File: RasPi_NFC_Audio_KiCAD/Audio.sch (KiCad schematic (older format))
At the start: 14 parts

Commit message: Schematic update
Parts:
- removed J?: SPKR0, Connector_PinHeader_2.54mm:PinHeader_1x02_P2.54mm_Vertical, symbol Connector_Generic:Conn_01x02
- removed J?: SPKR1, Connector_PinHeader_2.54mm:PinHeader_1x02_P2.54mm_Vertical, symbol Connector_Generic:Conn_01x02
- added J? (x2): Screw_Terminal_01x02, symbol Connector:Screw_Terminal_01x02
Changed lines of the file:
@@
 NoConn ~ 4590 2530
 $Comp
-L power:GND #PWR?
+L power:GND #PWR0134
 U 1 1 5ACDFE68
 P 5490 3280
-F 0 "#PWR?" H 5490 3030 50  0001 C CNN
+F 0 "#PWR0134" H 5490 3030 50  0001 C CNN
 F 1 "GND" H 5490 3130 50  0000 C CNN
 F 2 "" H 5490 3280 50  0001 C CNN
@@
 $EndComp
 $Comp
-L power:+5V #PWR?
+L power:+5V #PWR0135
 U 1 1 5ACDFE6E
 P 5540 1080
-F 0 "#PWR?" H 5540 930 50  0001 C CNN
+F 0 "#PWR0135" H 5540 930 50  0001 C CNN
 F 1 "+5V" H 5540 1220 50  0000 C CNN
 F 2 "" H 5540 1080 50  0001 C CNN
@@
 $EndComp
 $Comp
-L power:GND #PWR?
+L power:GND #PWR0136
 U 1 1 5ACDFE90
 P 3570 2440
-F 0 "#PWR?" H 3570 2190 50  0001 C CNN
+F 0 "#PWR0136" H 3570 2190 50  0001 C CNN
 F 1 "GND" H 3570 2290 50  0000 C CNN
 F 2 "" H 3570 2440 50  0001 C CNN
@@
 $EndComp
 $Comp
-L power:+5V #PWR?
+L power:+5V #PWR0137
 U 1 1 5ACDFE96
 P 3570 1640
-F 0 "#PWR?" H 3570 1490 50  0001 C CNN
+F 0 "#PWR0137" H 3570 1490 50  0001 C CNN
 F 1 "+5V" H 3570 1780 50  0000 C CNN
 F 2 "" H 3570 1640 50  0001 C CNN
@@
 $EndComp
 $Comp
-L power:GND #PWR?
+L power:GND #PWR0138
 U 1 1 5AD12414
 P 5820 1450
-F 0 "#PWR?" H 5820 1200 50  0001 C CNN
+F 0 "#PWR0138" H 5820 1200 50  0001 C CNN
 F 1 "GND" H 5820 1300 50  0000 C CNN
 F 2 "" H 5820 1450 50  0001 C CNN
@@
 $EndComp
 $Comp
-L power:GND #PWR?
+L power:GND #PWR0139
 U 1 1 5AD125D7
 P 6150 1460
-F 0 "#PWR?" H 6150 1210 50  0001 C CNN
+F 0 "#PWR0139" H 6150 1210 50  0001 C CNN
 F 1 "GND" H 6150 1310 50  0000 C CNN
 F 2 "" H 6150 1460 50  0001 C CNN
@@
 NoConn ~ 4590 5320
 $Comp
-L power:GND #PWR?
+L power:GND #PWR0140
 U 1 1 5CC75417
 P 5490 6070
-F 0 "#PWR?" H 5490 5820 50  0001 C CNN
+F 0 "#PWR0140" H 5490 5820 50  0001 C CNN
 F 1 "GND" H 5490 5920 50  0000 C CNN
 F 2 "" H 5490 6070 50  0001 C CNN
@@
 $EndComp
 $Comp
-L power:+5V #PWR?
+L power:+5V #PWR0141
 U 1 1 5CC7541D
 P 5540 3870
-F 0 "#PWR?" H 5540 3720 50  0001 C CNN
+F 0 "#PWR0141" H 5540 3720 50  0001 C CNN
 F 1 "+5V" H 5540 4010 50  0000 C CNN
 F 2 "" H 5540 3870 50  0001 C CNN
@@
 $EndComp
 $Comp
-L power:GND #PWR?
+L power:GND #PWR0142
 U 1 1 5CC75437
 P 3570 5230
-F 0 "#PWR?" H 3570 4980 50  0001 C CNN
+F 0 "#PWR0142" H 3570 4980 50  0001 C CNN
 F 1 "GND" H 3570 5080 50  0000 C CNN
 F 2 "" H 3570 5230 50  0001 C CNN
@@
 $EndComp
 $Comp
-L power:+5V #PWR?
+L power:+5V #PWR0143
 U 1 1 5CC7543D
 P 3570 4430
-F 0 "#PWR?" H 3570 4280 50  0001 C CNN
+F 0 "#PWR0143" H 3570 4280 50  0001 C CNN
 F 1 "+5V" H 3570 4570 50  0000 C CNN
 F 2 "" H 3570 4430 50  0001 C CNN
@@
 $EndComp
 $Comp
-L power:GND #PWR?
+L power:GND #PWR0144
 U 1 1 5CC7545E
 P 5820 4240
-F 0 "#PWR?" H 5820 3990 50  0001 C CNN
+F 0 "#PWR0144" H 5820 3990 50  0001 C CNN
 F 1 "GND" H 5820 4090 50  0000 C CNN
 F 2 "" H 5820 4240 50  0001 C CNN
@@
 $EndComp
 $Comp
-L power:GND #PWR?
+L power:GND #PWR0145
 U 1 1 5CC7546B
 P 6150 4250
-F 0 "#PWR?" H 6150 4000 50  0001 C CNN
+F 0 "#PWR0145" H 6150 4000 50  0001 C CNN
 F 1 "GND" H 6150 4100 50  0000 C CNN
 F 2 "" H 6150 4250 50  0001 C CNN
@@
 Wire Wire Line
 	3570 4820 3570 4880
-$Comp
-L Connector_Generic:Conn_01x02 J?
-U 1 1 5D28F8A3
-P 6710 2630
-AR Path="/5CF2E53C/5D28F8A3" Ref="J?"  Part="1"
-AR Path="/5CC5875B/5D28F8A3" Ref="J?"  Part="1"
-AR Path="/5E18E75B/5D28F8A3" Ref="J?"  Part="1"
-F 0 "J?" H 6790 2622 50  0000 L CNN
-F 1 "SPKR0" H 6790 2531 50  0000 L CNN
-F 2 "Connector_PinHeader_2.54mm:PinHeader_1x02_P2.54mm_Vertical" H 6710 2630 50  0001 C CNN
-F 3 "~" H 6710 2630 50  0001 C CNN
-	1    6710 2630
-	1    0    0    -1
-$EndComp
 Wire Wire Line
 	6390 2630 6510 2630
 Wire Wire Line
 	6390 2730 6510 2730
-$Comp
-L Connector_Generic:Conn_01x02 J?
-U 1 1 5D29A4BB
-P 6750 5420
-AR Path="/5CF2E53C/5D29A4BB" Ref="J?"  Part="1"
-AR Path="/5CC5875B/5D29A4BB" Ref="J?"  Part="1"
-AR Path="/5E18E75B/5D29A4BB" Ref="J?"  Part="1"
-F 0 "J?" H 6830 5412 50  0000 L CNN
-F 1 "SPKR1" H 6830 5321 50  0000 L CNN
-F 2 "Connector_PinHeader_2.54mm:PinHeader_1x02_P2.54mm_Vertical" H 6750 5420 50  0001 C CNN
-F 3 "~" H 6750 5420 50  0001 C CNN
-	1    6750 5420
-	1    0    0    -1
-$EndComp
 Wire Wire Line
 	6390 5420 6550 5420
@@
 $EndComp
 $Comp
-L power:+5V #PWR?
+L power:+5V #PWR0146
 U 1 1 5E1DB377
 P 4380 1530
-F 0 "#PWR?" H 4380 1380 50  0001 C CNN
+F 0 "#PWR0146" H 4380 1380 50  0001 C CNN
 F 1 "+5V" H 4380 1670 50  0000 C CNN
 F 2 "" H 4380 1530 50  0001 C CNN
@@
 $EndComp
 $Comp
-L power:+5V #PWR?
+L power:+5V #PWR0147
 U 1 1 5E1F1D9F
 P 4450 4280
-F 0 "#PWR?" H 4450 4130 50  0001 C CNN
+F 0 "#PWR0147" H 4450 4130 50  0001 C CNN
 F 1 "+5V" H 4450 4420 50  0000 C CNN
 F 2 "" H 4450 4280 50  0001 C CNN
@@
 Wire Wire Line
 	4450 4630 4450 4920
+$Comp
+L Connector:Screw_Terminal_01x02 J?
+U 1 1 5E2A07D2
+P 6710 2630
+F 0 "J?" H 6790 2622 50  0000 L CNN
+F 1 "Screw_Terminal_01x02" H 6790 2531 50  0000 L CNN
+F 2 "" H 6710 2630 50  0001 C CNN
+F 3 "~" H 6710 2630 50  0001 C CNN
+	1    6710 2630
+	1    0    0    -1
+$EndComp
+$Comp
+L Connector:Screw_Terminal_01x02 J?
+U 1 1 5E2A25ED
+P 6750 5420
+F 0 "J?" H 6830 5412 50  0000 L CNN
+F 1 "Screw_Terminal_01x02" H 6830 5321 50  0000 L CNN
+F 2 "" H 6750 5420 50  0001 C CNN
+F 3 "~" H 6750 5420 50  0001 C CNN
+	1    6750 5420
+	1    0    0    -1
+$EndComp
 $EndSCHEMATC

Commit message: Schematic Updates
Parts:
- C? (x2): DigiKey (none) -> 1276-1119-1-ND; Part # (none) -> CL10A106MQ8NNNC
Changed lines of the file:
@@
 F 2 "Capacitor_SMD:C_0603_1608Metric_Pad1.05x0.95mm_HandSolder" H 6188 1120 50  0001 C CNN
 F 3 "" H 6150 1270 50  0001 C CNN
+F 4 "CL10A106MQ8NNNC" H 6150 1270 50  0001 C CNN "Part #"
+F 5 "1276-1119-1-ND" H 6150 1270 50  0001 C CNN "DigiKey"
 	1    6150 1270
 	1    0    0    -1
@@
 F 2 "Capacitor_SMD:C_0603_1608Metric_Pad1.05x0.95mm_HandSolder" H 6188 3910 50  0001 C CNN
 F 3 "" H 6150 4060 50  0001 C CNN
+F 4 "CL10A106MQ8NNNC" H 6150 4060 50  0001 C CNN "Part #"
+F 5 "1276-1119-1-ND" H 6150 4060 50  0001 C CNN "DigiKey"
 	1    6150 4060
 	1    0    0    -1

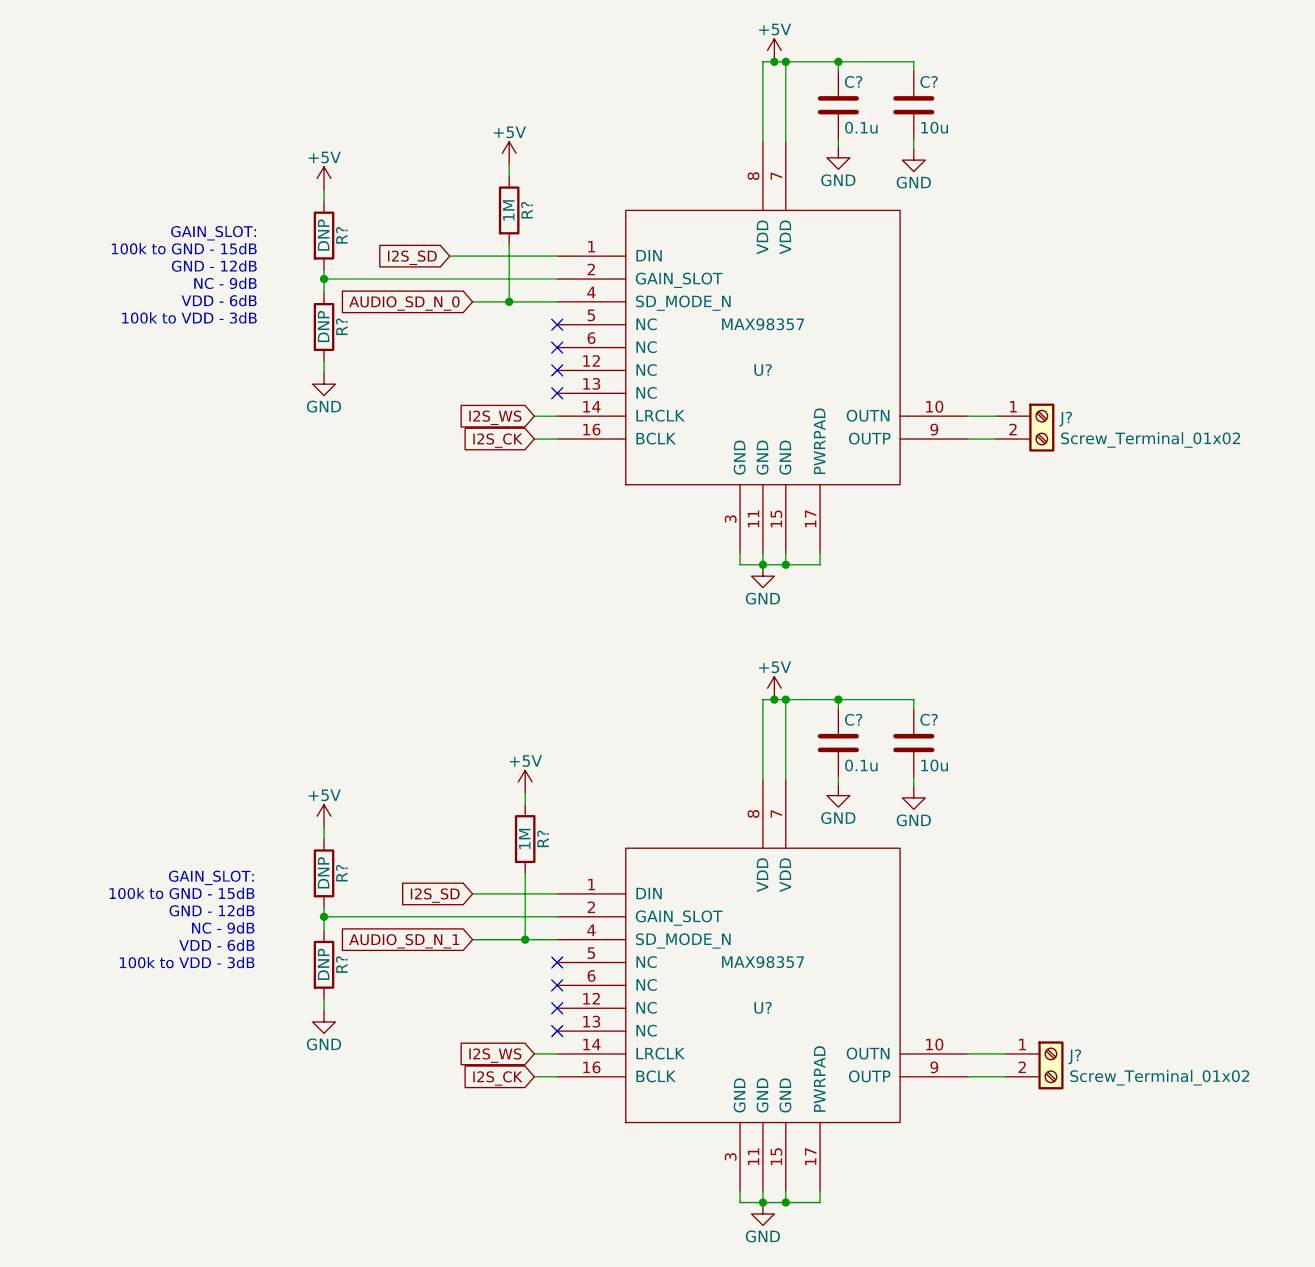
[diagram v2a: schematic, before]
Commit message: Schematic Updates
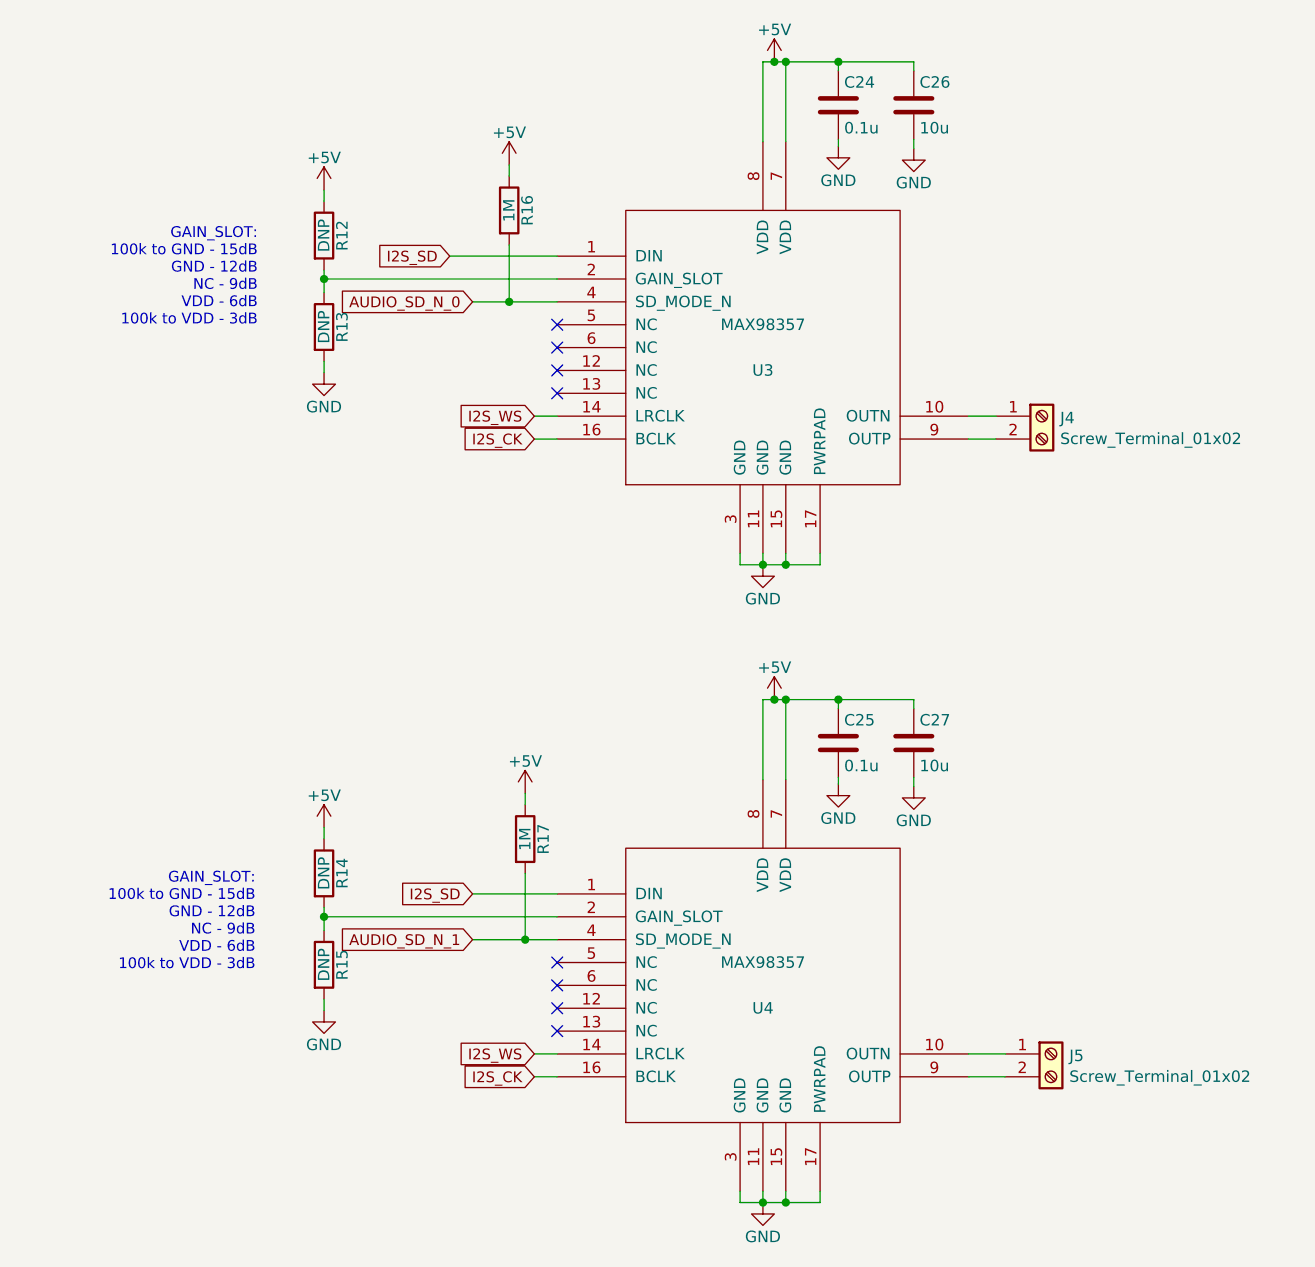
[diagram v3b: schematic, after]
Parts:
- gave numbers to parts that had none: 14
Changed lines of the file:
@@
 $EndDescr
 $Comp
-L MAX98357:MAX98357 U?
+L MAX98357:MAX98357 U3
 U 1 1 5ACDFE57
 P 5490 2330
-F 0 "U?" H 5490 2230 50  0000 C CNN
+F 0 "U3" H 5490 2230 50  0000 C CNN
 F 1 "MAX98357" H 5490 2430 50  0000 C CNN
 F 2 "CommandCenter:QFN50P300X300X80-17N" H 5490 2330 50  0001 C CNN
@@
 AUDIO_SD_N_0
 $Comp
-L Device:R R?
+L Device:R R12
 U 1 1 5ACDFE7F
 P 3570 1840
-F 0 "R?" V 3650 1840 50  0000 C CNN
+F 0 "R12" V 3650 1840 50  0000 C CNN
 F 1 "DNP" V 3570 1840 50  0000 C CNN
 F 2 "Resistor_SMD:R_0603_1608Metric_Pad1.05x0.95mm_HandSolder" V 3500 1840 50  0001 C CNN
@@
 $EndComp
 $Comp
-L Device:R R?
+L Device:R R13
 U 1 1 5ACDFE86
 P 3570 2240
-F 0 "R?" V 3650 2240 50  0000 C CNN
+F 0 "R13" V 3650 2240 50  0000 C CNN
 F 1 "DNP" V 3570 2240 50  0000 C CNN
 F 2 "Resistor_SMD:R_0603_1608Metric_Pad1.05x0.95mm_HandSolder" V 3500 2240 50  0001 C CNN
@@
 GAIN_SLOT:\n    100k to GND - 15dB\n    GND - 12dB\n    NC - 9dB\n    VDD - 6dB\n    100k to VDD - 3dB
 $Comp
-L Device:C C?
+L Device:C C24
 U 1 1 5AD1240E
 P 5820 1270
-F 0 "C?" H 5845 1370 50  0000 L CNN
+F 0 "C24" H 5845 1370 50  0000 L CNN
 F 1 "0.1u" H 5845 1170 50  0000 L CNN
 F 2 "Capacitor_SMD:C_0603_1608Metric_Pad1.05x0.95mm_HandSolder" H 5858 1120 50  0001 C CNN
@@
 	5820 1420 5820 1450
 $Comp
-L Device:C C?
+L Device:C C26
 U 1 1 5AD12566
 P 6150 1270
-F 0 "C?" H 6175 1370 50  0000 L CNN
+F 0 "C26" H 6175 1370 50  0000 L CNN
 F 1 "10u" H 6175 1170 50  0000 L CNN
 F 2 "Capacitor_SMD:C_0603_1608Metric_Pad1.05x0.95mm_HandSolder" H 6188 1120 50  0001 C CNN
@@
 	3570 2030 3570 2090
 $Comp
-L MAX98357:MAX98357 U?
+L MAX98357:MAX98357 U4
 U 1 1 5CC75407
 P 5490 5120
-F 0 "U?" H 5490 5020 50  0000 C CNN
+F 0 "U4" H 5490 5020 50  0000 C CNN
 F 1 "MAX98357" H 5490 5220 50  0000 C CNN
 F 2 "CommandCenter:QFN50P300X300X80-17N" H 5490 5120 50  0001 C CNN
@@
 AUDIO_SD_N_1
 $Comp
-L Device:R R?
+L Device:R R14
 U 1 1 5CC7542B
 P 3570 4630
-F 0 "R?" V 3650 4630 50  0000 C CNN
+F 0 "R14" V 3650 4630 50  0000 C CNN
 F 1 "DNP" V 3570 4630 50  0000 C CNN
 F 2 "Resistor_SMD:R_0603_1608Metric_Pad1.05x0.95mm_HandSolder" V 3500 4630 50  0001 C CNN
@@
 $EndComp
 $Comp
-L Device:R R?
+L Device:R R15
 U 1 1 5CC75431
 P 3570 5030
-F 0 "R?" V 3650 5030 50  0000 C CNN
+F 0 "R15" V 3650 5030 50  0000 C CNN
 F 1 "DNP" V 3570 5030 50  0000 C CNN
 F 2 "Resistor_SMD:R_0603_1608Metric_Pad1.05x0.95mm_HandSolder" V 3500 5030 50  0001 C CNN
@@
 GAIN_SLOT:\n    100k to GND - 15dB\n    GND - 12dB\n    NC - 9dB\n    VDD - 6dB\n    100k to VDD - 3dB
 $Comp
-L Device:C C?
+L Device:C C25
 U 1 1 5CC75458
 P 5820 4060
-F 0 "C?" H 5845 4160 50  0000 L CNN
+F 0 "C25" H 5845 4160 50  0000 L CNN
 F 1 "0.1u" H 5845 3960 50  0000 L CNN
 F 2 "Capacitor_SMD:C_0603_1608Metric_Pad1.05x0.95mm_HandSolder" H 5858 3910 50  0001 C CNN
@@
 	5820 4210 5820 4240
 $Comp
-L Device:C C?
+L Device:C C27
 U 1 1 5CC75465
 P 6150 4060
-F 0 "C?" H 6175 4160 50  0000 L CNN
+F 0 "C27" H 6175 4160 50  0000 L CNN
 F 1 "10u" H 6175 3960 50  0000 L CNN
 F 2 "Capacitor_SMD:C_0603_1608Metric_Pad1.05x0.95mm_HandSolder" H 6188 3910 50  0001 C CNN
@@
 	4220 2130 4380 2130
 $Comp
-L Device:R R?
+L Device:R R16
 U 1 1 5E1DB371
 P 4380 1730
-F 0 "R?" V 4460 1730 50  0000 C CNN
+F 0 "R16" V 4460 1730 50  0000 C CNN
 F 1 "1M" V 4380 1730 50  0000 C CNN
 F 2 "Resistor_SMD:R_0603_1608Metric_Pad1.05x0.95mm_HandSolder" V 4310 1730 50  0001 C CNN
@@
 	4220 4920 4450 4920
 $Comp
-L Device:R R?
+L Device:R R17
 U 1 1 5E1F1D99
 P 4450 4480
-F 0 "R?" V 4530 4480 50  0000 C CNN
+F 0 "R17" V 4530 4480 50  0000 C CNN
 F 1 "1M" V 4450 4480 50  0000 C CNN
 F 2 "Resistor_SMD:R_0603_1608Metric_Pad1.05x0.95mm_HandSolder" V 4380 4480 50  0001 C CNN
@@
 	4450 4630 4450 4920
 $Comp
-L Connector:Screw_Terminal_01x02 J?
+L Connector:Screw_Terminal_01x02 J4
 U 1 1 5E2A07D2
 P 6710 2630
-F 0 "J?" H 6790 2622 50  0000 L CNN
+F 0 "J4" H 6790 2622 50  0000 L CNN
 F 1 "Screw_Terminal_01x02" H 6790 2531 50  0000 L CNN
 F 2 "" H 6710 2630 50  0001 C CNN
@@
 $EndComp
 $Comp
-L Connector:Screw_Terminal_01x02 J?
+L Connector:Screw_Terminal_01x02 J5
 U 1 1 5E2A25ED
 P 6750 5420
-F 0 "J?" H 6830 5412 50  0000 L CNN
+F 0 "J5" H 6830 5412 50  0000 L CNN
 F 1 "Screw_Terminal_01x02" H 6830 5321 50  0000 L CNN
 F 2 "" H 6750 5420 50  0001 C CNN

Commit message: Schematic updates
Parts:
- C24, C25: DigiKey (none) -> 1276-1000-1-ND; Part # (none) -> CL10B104KB8NNNC
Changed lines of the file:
@@
 F 2 "Capacitor_SMD:C_0603_1608Metric_Pad1.05x0.95mm_HandSolder" H 5858 1120 50  0001 C CNN
 F 3 "" H 5820 1270 50  0001 C CNN
+F 4 "CL10B104KB8NNNC" H 5820 1270 50  0001 C CNN "Part #"
+F 5 "1276-1000-1-ND" H 5820 1270 50  0001 C CNN "DigiKey"
 	1    5820 1270
 	1    0    0    -1
@@
 F 2 "Capacitor_SMD:C_0603_1608Metric_Pad1.05x0.95mm_HandSolder" H 5858 3910 50  0001 C CNN
 F 3 "" H 5820 4060 50  0001 C CNN
+F 4 "CL10B104KB8NNNC" H 5820 4060 50  0001 C CNN "Part #"
+F 5 "1276-1000-1-ND" H 5820 4060 50  0001 C CNN "DigiKey"
 	1    5820 4060
 	1    0    0    -1
